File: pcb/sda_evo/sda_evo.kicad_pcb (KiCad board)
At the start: 4 copper layers, 61.5 x 105.2 mm, 136 parts, among them J1 PROG, J10 SPKR, J11 AudioJack, J2 USB_C_Receptacle_USB2.0, J3 Conn_01x40, J4 INT_EXP, J5 BATT, J9 Micro_SD_Card_Det, Q1 IRLML6302, SW1 RESET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

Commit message: Adaded part mockups. PCB is nearly finished.
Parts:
- added C52: 100n, Capacitor_SMD:C_0805_2012Metric_Pad1.18x1.45mm_HandSolder, B.Cu at (89.4, 126.1)
- added C53: 4.7u, Capacitor_SMD:C_0805_2012Metric_Pad1.18x1.45mm_HandSolder, B.Cu at (91.6, 126.1)
- C22, C23: value ?? -> 12,5p
- C3, C4: value ?? -> 12p
- J2: footprint Connector_USB:USB_C_Receptacle_XKB_U262-16XN-4BVC11 -> sda-parts:USB_C
- SW1: footprint Button_Switch_SMD:SW_SPST_B3S-1000 -> Button_Switch_SMD:SW_SPST_PTS645
- TP2: value TP_VUSB -> VUSB
- moved R11 17.5 mm to (80.2, 143.4)
- moved R10 13.0 mm to (78.2, 143.4)
- moved D5 10.3 mm to (66.8, 143.8)
- moved R9 8.45 mm to (76.2, 143.4), turned to 90 degrees
- moved TP1 7.81 mm to (81.2, 94.0)
- moved C23 4.46 mm to (97.1, 109.8)
- moved C47 4.35 mm to (62.3, 64.6), turned to 180 degrees
- moved R25 4.20 mm to (62.2, 60.4), turned to 0 degrees
- moved TP2 3.60 mm to (88.6, 134.8)
- moved TP3 2.75 mm to (85.0, 134.8)
- moved D3 2.52 mm to (80.5, 139.9), turned to 0 degrees
- moved C22 2.07 mm to (99.1, 109.8)
- moved Y2 2.07 mm to (101.4, 112.9)
- moved U9 1.88 mm to (73.0, 129.9)
- moved J9 1.80 mm to (104.5, 49.0)
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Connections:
- U10 pad 127: LCD_RST -> unconnected-(U10-PG12-Pad127)
- U10 pad 128: LCD_RD -> unconnected-(U10-PG13-Pad128)
- U10 pad 129: LCD_WR -> unconnected-(U10-PG14-Pad129)
- U10 pad 132: LCD_RS -> unconnected-(U10-PG15-Pad132)
- U10 pad 134: HALL_SENSE_R -> unconnected-(U10-PB4-Pad134)
- U10 pad 139: TS_P1 -> unconnected-(U10-PB8-Pad139)
- U10 pad 140: TS_P2 -> unconnected-(U10-PB9-Pad140)
- U10 pad 26: BTN_A -> BTN_B
- U10 pad 27: BTN_B -> BTN_A
- U10 pad 4: unconnected-(U10-PE5-Pad4) -> LCD_CS
- U10 pad 56: SIDE_BTN_4 -> TS_P1
- U10 pad 57: SIDE_BTN_5 -> TS_P2
- U10 pad 58: unconnected-(U10-PE7-Pad58) -> LCD_RST
- U10 pad 59: unconnected-(U10-PE8-Pad59) -> LCD_RD
- U10 pad 60: unconnected-(U10-PE9-Pad60) -> LCD_WR
- U10 pad 63: unconnected-(U10-PE10-Pad63) -> LCD_RS
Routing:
- net +3V3: track 0.00 -> 459.5 mm, vias 0 -> 18
- net GND: track 0.00 -> 199.2 mm, vias 0 -> 68
- net VBUS: track 0.00 -> 91.6 mm, vias 0 -> 3
- net BTN_A: track 0.00 -> 87.2 mm, vias 0 -> 1
- net RESET: track 0.00 -> 84.6 mm, vias 0 -> 3
- net BTN_UP: track 0.00 -> 84.1 mm, vias 0 -> 1
- net +BATT: track 0.00 -> 83.7 mm, vias 0 -> 5
- net BTN_DOWN: track 0.00 -> 82.9 mm, vias 0 -> 1
- net BTN_RIGHT: track 0.00 -> 78.3 mm, vias 0 -> 1
- net BTN_B: track 0.00 -> 74.8 mm, vias 0 -> 1
- net ISP_SWDIO: track 0.00 -> 69.9 mm, vias 0 -> 2
- net VD: track 0.00 -> 69.5 mm, vias 0 -> 2
- net ISP_SWCLK: track 0.00 -> 69.1 mm, vias 0 -> 2
- net BTN_LEFT: track 0.00 -> 63.3 mm, vias 0 -> 1
- net EXT_IO2: track 0.00 -> 61.8 mm, vias 0 -> 3
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- added copper zone on B.Cu, net GND
- added copper zone on F.Cu, net GND
- added copper zone on In1.Cu, net GND
- added copper zone on In2.Cu, net GND
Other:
- board text added: "Beta 0 IV. 2024 Designed in Budweis by Standa"
- board text removed: "Beta 0 Designed in Budweis by Standa"

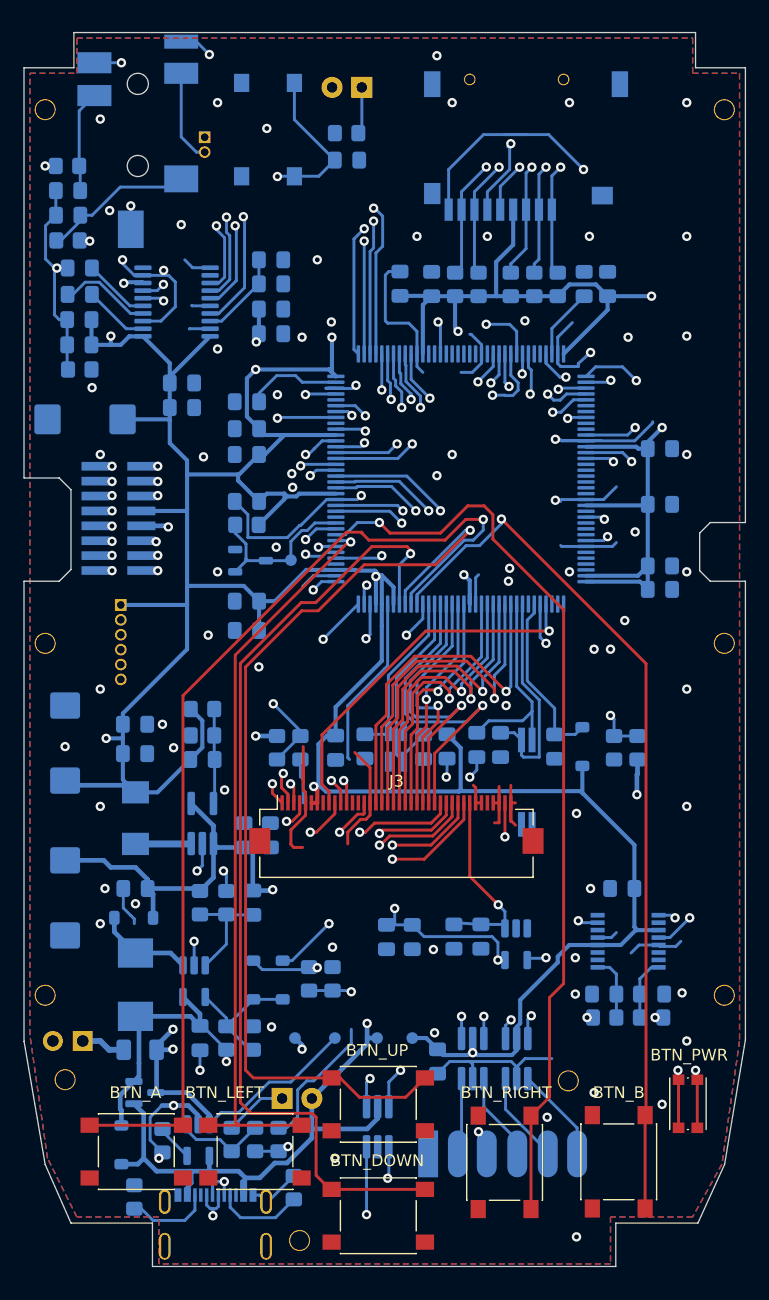
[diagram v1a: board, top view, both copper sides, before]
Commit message: i2s vias lenght matched
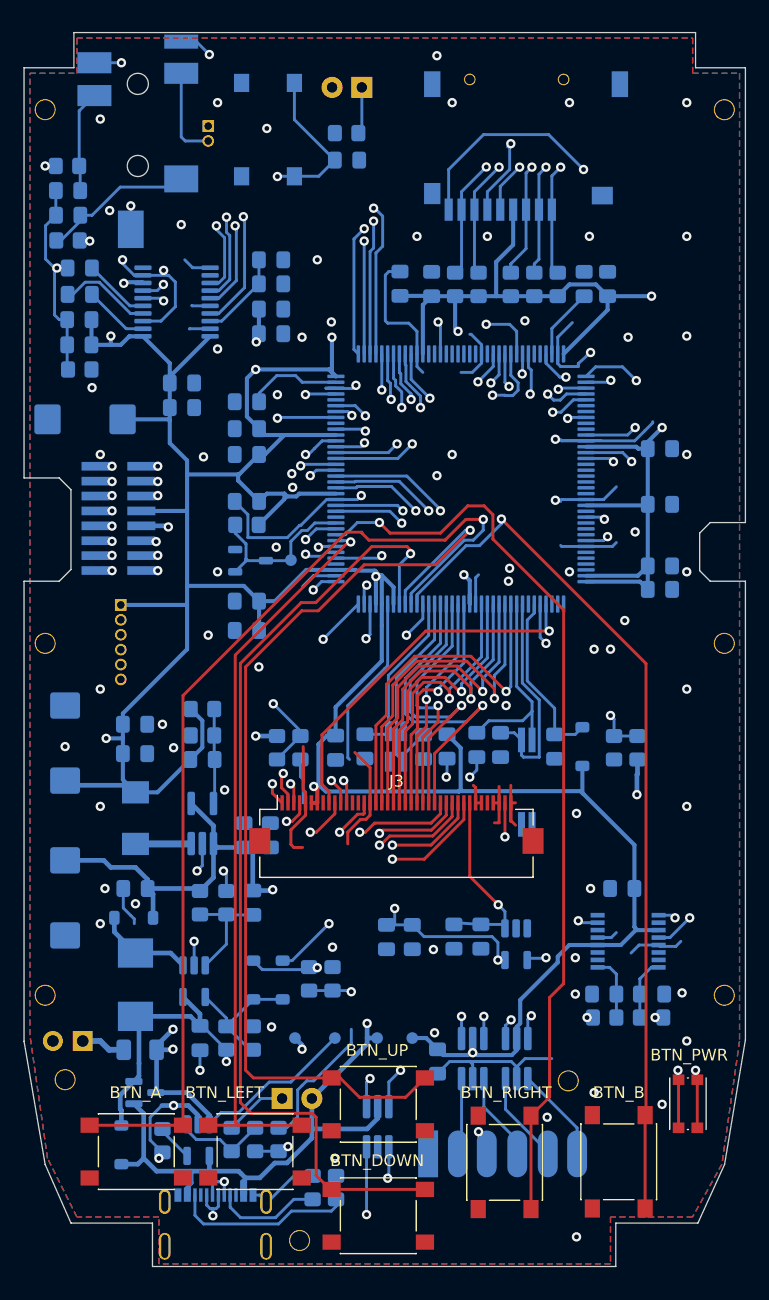
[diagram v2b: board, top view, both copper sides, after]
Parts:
- moved R28 17.2 mm to (85.1, 147.5)
- moved R29 1.60 mm to (83.1, 147.5)
- moved J10 1.00 mm to (74.2, 57.0)
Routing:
- net Net-(J2-CC2): track 7.24 -> 15.3 mm
- net PCM_CK: track 28.9 -> 33.4 mm
- net PCM_WS: track 29.9 -> 33.4 mm
- net SD_DETECT: track 40.4 -> 38.6 mm
- net Net-(J2-CC1): track 7.48 -> 9.08 mm
- net GNDA: track 54.7 -> 55.7 mm
- net PCM_MUTE: track 32.6 -> 33.4 mm
- net Net-(J10-Pin_1): track 23.3 -> 24.0 mm

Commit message: 3.5 jack moved a bit, added few holes to the casing
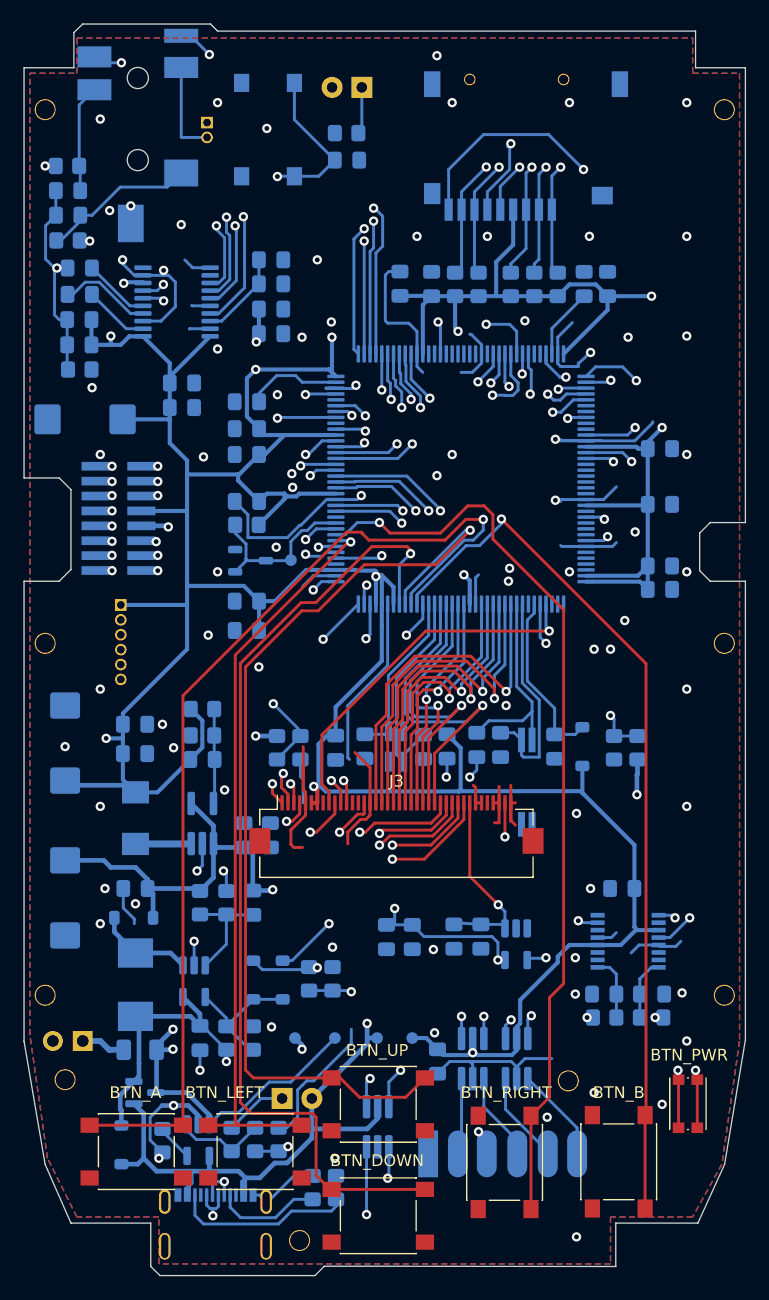
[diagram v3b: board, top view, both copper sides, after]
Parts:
- moved J11 0.50 mm to (68.2, 48.6)
- moved J10 0.32 mm to (74.1, 56.7)
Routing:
- net GNDA: track 55.7 -> 56.2 mm
- net Net-(C45-Pad1): track 8.67 -> 9.17 mm
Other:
- board size 61.5 x 105.2 mm -> 61.5 x 106.7 mm
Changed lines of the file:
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@@
   )
   (footprint "Connector_PinHeader_1.27mm:PinHeader_1x02_P1.27mm_Vertical" (layer "B.Cu")
-    (at 74.2 57 180)
+    (at 74.1 56.7 180)
     (descr "Through hole straight pin header, 1x02, 1.27mm pitch, single row")
     (tags "Through hole pin header THT 1x02 1.27mm single row")
@@
   )
   (footprint "sda-parts:3.5 Jack" (layer "B.Cu")
-    (at 68.2 49.1 90)
+    (at 68.2 48.6 90)
     (property "Sheetfile" "sda_evo.kicad_sch")
     (property "Sheetname" "")
@@
   (gr_line (start 62.75 49.025) (end 62.75 52.025)
     (stroke (width 0.1) (type default)) (layer "Edge.Cuts"))
-  (gr_line (start 69.45 150.525) (end 69.45 154.225)
+  (gr_line (start 75 48.9) (end 74.4 48.3)
+    (stroke (width 0.1) (type default)) (layer "Edge.Cuts"))
+  (gr_line (start 69.3 150.525) (end 69.3 154.225)
     (stroke (width 0.1) (type default)) (layer "Edge.Cuts"))
   (gr_line (start 116.1 91.7) (end 116.1 94.9)
@@
   (gr_line (start 118.225 145.525) (end 120 134.9)
     (stroke (width 0.1) (type default)) (layer "Edge.Cuts"))
+  (gr_line (start 84.1 154.2) (end 83.3 155)
+    (stroke (width 0.1) (type default)) (layer "Edge.Cuts"))
   (gr_line (start 60.3 145.525) (end 62.5 150.525)
     (stroke (width 0.1) (type default)) (layer "Edge.Cuts"))
@@
   (gr_line (start 58.5 135.025) (end 60.3 145.525)
     (stroke (width 0.1) (type default)) (layer "Edge.Cuts"))
+  (gr_line (start 83.3 155) (end 70.1 155)
+    (stroke (width 0.1) (type default)) (layer "Edge.Cuts"))
+  (gr_line (start 70.1 155) (end 69.3 154.225)
+    (stroke (width 0.1) (type default)) (layer "Edge.Cuts"))
   (gr_line (start 108.95 150.525) (end 115.95 150.525)
     (stroke (width 0.1) (type default)) (layer "Edge.Cuts"))
-  (gr_line (start 62.75 49.025) (end 115.75 49.025)
+  (gr_line (start 75 48.9) (end 115.75 48.9)
     (stroke (width 0.1) (type default)) (layer "Edge.Cuts"))
   (gr_line (start 115.95 150.525) (end 118.225 145.525)
@@
   (gr_line (start 58.5 52.025) (end 58.5 87)
     (stroke (width 0.1) (type default)) (layer "Edge.Cuts"))
-  (gr_line (start 115.75 49.025) (end 115.75 52.025)
+  (gr_line (start 74.4 48.3) (end 63.5 48.3)
+    (stroke (width 0.1) (type default)) (layer "Edge.Cuts"))
+  (gr_line (start 115.75 48.9) (end 115.75 52.025)
     (stroke (width 0.1) (type default)) (layer "Edge.Cuts"))
   (gr_line (start 115.75 52.025) (end 120 52.025)
     (stroke (width 0.1) (type default)) (layer "Edge.Cuts"))
-  (gr_line (start 62.5 150.525) (end 69.45 150.525)
+  (gr_line (start 62.5 150.525) (end 69.3 150.525)
+    (stroke (width 0.1) (type default)) (layer "Edge.Cuts"))
+  (gr_line (start 63.5 48.3) (end 62.75 49.025)
     (stroke (width 0.1) (type default)) (layer "Edge.Cuts"))
   (gr_line (start 117 95.8) (end 120 95.8)
@@
   (gr_line (start 58.5 95.8) (end 58.5 135.025)
     (stroke (width 0.1) (type default)) (layer "Edge.Cuts"))
-  (gr_line (start 69.45 154.225) (end 108.95 154.225)
+  (gr_line (start 84.1 154.2) (end 108.95 154.225)
     (stroke (width 0.1) (type default)) (layer "Edge.Cuts"))
   (gr_line (start 120 90.8) (end 117 90.8)
@@
   (segment (start 62 68.4) (end 61.3 69.1) (width 0.25) (layer "In1.Cu") (net 16))
   (segment (start 66.9 68.4) (end 62 68.4) (width 0.25) (layer "In1.Cu") (net 16))
-  (segment (start 73.9 58.57) (end 74.2 58.27) (width 0.25) (layer "In2.Cu") (net 16))
-  (segment (start 73.9 65.8) (end 73.9 58.57) (width 0.25) (layer "In2.Cu") (net 16))
+  (segment (start 73.9 58.17) (end 74.1 57.97) (width 0.25) (layer "In2.Cu") (net 16))
   (segment (start 70.4 69.3) (end 73.9 65.8) (width 0.25) (layer "In2.Cu") (net 16))
+  (segment (start 73.9 65.8) (end 73.9 58.17) (width 0.25) (layer "In2.Cu") (net 16))
   (segment (start 61.225 64.6) (end 60.335 65.49) (width 0.25) (layer "B.Cu") (net 16))
   (segment (start 68.6375 69.725) (end 70.825 69.725) (width 0.25) (layer "B.Cu") (net 16))
@@
   (segment (start 61.2125 64.5875) (end 61.225 64.6) (width 0.25) (layer "B.Cu") (net 16))
   (segment (start 61.5 73.5) (end 62.175 73.5) (width 0.25) (layer "B.Cu") (net 16))
+  (segment (start 71.9 57.927106) (end 71.942894 57.97) (width 0.25) (layer "B.Cu") (net 16))
+  (segment (start 71.9 52) (end 71.9 57.927106) (width 0.25) (layer "B.Cu") (net 16))
   (segment (start 62.175 73.5) (end 62.175 75.65) (width 0.25) (layer "B.Cu") (net 16))
-  (segment (start 72.242894 58.27) (end 74.2 58.27) (width 0.25) (layer "B.Cu") (net 16))
   (segment (start 61.25 69.25) (end 61.625 69.25) (width 0.25) (layer "B.Cu") (net 16))
-  (segment (start 71.9 57.927106) (end 72.242894 58.27) (width 0.25) (layer "B.Cu") (net 16))
-  (segment (start 71.9 52.5) (end 71.9 57.927106) (width 0.25) (layer "B.Cu") (net 16))
   (segment (start 62.2125 69.1) (end 62.0625 69.25) (width 0.25) (layer "B.Cu") (net 16))
   (segment (start 61.2125 62.5) (end 61.2125 64.5875) (width 0.25) (layer "B.Cu") (net 16))
@@
   (segment (start 62.0625 69.25) (end 61.625 69.25) (width 0.25) (layer "B.Cu") (net 16))
   (segment (start 70.825 69.725) (end 71.4 70.3) (width 0.25) (layer "B.Cu") (net 16))
+  (segment (start 71.942894 57.97) (end 74.1 57.97) (width 0.25) (layer "B.Cu") (net 16))
   (segment (start 62.175 77.675) (end 62.25 77.75) (width 0.25) (layer "B.Cu") (net 16))
   (segment (start 61.05 69.25) (end 61.1 69.3) (width 0.25) (layer "B.Cu") (net 16))
@@
   (segment (start 73.7125 133.7125) (end 75.75 135.75) (width 0.25) (layer "B.Cu") (net 20))
   (segment (start 66.8 142.2) (end 66.8 140.9) (width 0.4) (layer "B.Cu") (net 20))
+  (segment (start 63.2 55.2) (end 64.5 53.9) (width 0.25) (layer "B.Cu") (net 21))
   (segment (start 63.2875 60.4875) (end 63.2 60.4) (width 0.25) (layer "B.Cu") (net 21))
   (segment (start 63.2875 62.5) (end 63.2875 60.4875) (width 0.25) (layer "B.Cu") (net 21))
-  (segment (start 63.2 55.7) (end 64.5 54.4) (width 0.25) (layer "B.Cu") (net 21))
-  (segment (start 63.2 60.4) (end 63.2 55.7) (width 0.25) (layer "B.Cu") (net 21))
+  (segment (start 63.2 60.4) (end 63.2 55.2) (width 0.25) (layer "B.Cu") (net 21))
   (segment (start 74.75 111) (end 74.75 114.65) (width 0.25) (layer "B.Cu") (net 22))
   (segment (start 74.7125 110.9625) (end 74.75 111) (width 0.25) (layer "B.Cu") (net 22))
@@
   (segment (start 61.25 66.75) (end 61.644042 66.75) (width 0.25) (layer "B.Cu") (net 23))
   (segment (start 63.3 65.094042) (end 63.3 64.6) (width 0.25) (layer "B.Cu") (net 23))
+  (segment (start 70.7 62.2) (end 71.9 61) (width 0.25) (layer "B.Cu") (net 23))
   (segment (start 61.644042 66.75) (end 63.3 65.094042) (width 0.25) (layer "B.Cu") (net 23))
-  (segment (start 66.7 62.2) (end 71.2 62.2) (width 0.25) (layer "B.Cu") (net 23))
   (segment (start 63.3 64.6) (end 64.3 64.6) (width 0.25) (layer "B.Cu") (net 23))
-  (segment (start 71.2 62.2) (end 71.9 61.5) (width 0.25) (layer "B.Cu") (net 23))
   (segment (start 64.3 64.6) (end 66.7 62.2) (width 0.25) (layer "B.Cu") (net 23))
+  (segment (start 66.7 62.2) (end 70.7 62.2) (width 0.25) (layer "B.Cu") (net 23))
   (segment (start 73.5 124.2125) (end 75.75 124.2125) (width 0.25) (layer "B.Cu") (net 24))
   (segment (start 73.95 128.55) (end 75.75 126.75) (width 0.25) (layer "B.Cu") (net 24))
@@
   (via (at 66.8 51.6) (size 0.8) (drill 0.4) (layers "F.Cu" "B.Cu") (net 91))
   (via (at 67.6 63.8) (size 0.8) (drill 0.4) (layers "F.Cu" "B.Cu") (net 91))
+  (segment (start 71.1 57.95) (end 72.85 57.95) (width 0.25) (layer "In1.Cu") (net 91))
   (segment (start 68.8 63.8) (end 71.1 61.5) (width 0.25) (layer "In1.Cu") (net 91))
-  (segment (start 73.25 57.95) (end 74.2 57) (width 0.25) (layer "In1.Cu") (net 91))
   (segment (start 66.8 51.6) (end 66.8 53.803122) (width 0.25) (layer "In1.Cu") (net 91))
   (segment (start 71.1 61.5) (end 71.1 57.95) (width 0.25) (layer "In1.Cu") (net 91))
+  (segment (start 72.85 57.95) (end 74.1 56.7) (width 0.25) (layer "In1.Cu") (net 91))
   (segment (start 66.8 53.803122) (end 70.946878 57.95) (width 0.25) (layer "In1.Cu") (net 91))
   (segment (start 70.946878 57.95) (end 71.1 57.95) (width 0.25) (layer "In1.Cu") (net 91))
-  (segment (start 71.1 57.95) (end 73.25 57.95) (width 0.25) (layer "In1.Cu") (net 91))
   (segment (start 67.6 63.8) (end 68.8 63.8) (width 0.25) (layer "In1.Cu") (net 91))
-  (segment (start 64.5 51.6) (end 66.8 51.6) (width 0.25) (layer "B.Cu") (net 91))
-  (segment (start 67.6 65.8) (end 67.6 63.8) (width 0.25) (layer "B.Cu") (net 91))
+  (segment (start 67.6 65.3) (end 67.6 63.8) (width 0.25) (layer "B.Cu") (net 91))
+  (segment (start 64.5 51.1) (end 65 51.6) (width 0.25) (layer "B.Cu") (net 91))
+  (segment (start 65 51.6) (end 66.8 51.6) (width 0.25) (layer "B.Cu") (net 91))
   (via (at 93.7 51) (size 0.8) (drill 0.4) (layers "F.Cu" "B.Cu") (net 92))
   (via (at 97.9 73.9) (size 0.8) (drill 0.4) (layers "F.Cu" "B.Cu") (net 92))
@@
   (segment (start 97.9 73.9) (end 93.7 69.7) (width 0.25) (layer "In2.Cu") (net 92))
   (segment (start 93.7 69.7) (end 93.7 51) (width 0.25) (layer "In2.Cu") (net 92))
-  (segment (start 71.9 49.8) (end 73.2 49.8) (width 0.25) (layer "B.Cu") (net 92))
+  (segment (start 72.7 49.3) (end 74.3 50.9) (width 0.25) (layer "B.Cu") (net 92))
+  (segment (start 71.9 49.3) (end 72.7 49.3) (width 0.25) (layer "B.Cu") (net 92))
   (segment (start 100.5 74.5) (end 100.5 76.425) (width 0.25) (layer "B.Cu") (net 92))
-  (segment (start 73.2 49.8) (end 74.3 50.9) (width 0.25) (layer "B.Cu") (net 92))
   (segment (start 99.9 73.9) (end 100.5 74.5) (width 0.25) (layer "B.Cu") (net 92))
   (segment (start 97.9 73.9) (end 99.9 73.9) (width 0.25) (layer "B.Cu") (net 92))

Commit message: PCB: footprints adjusted
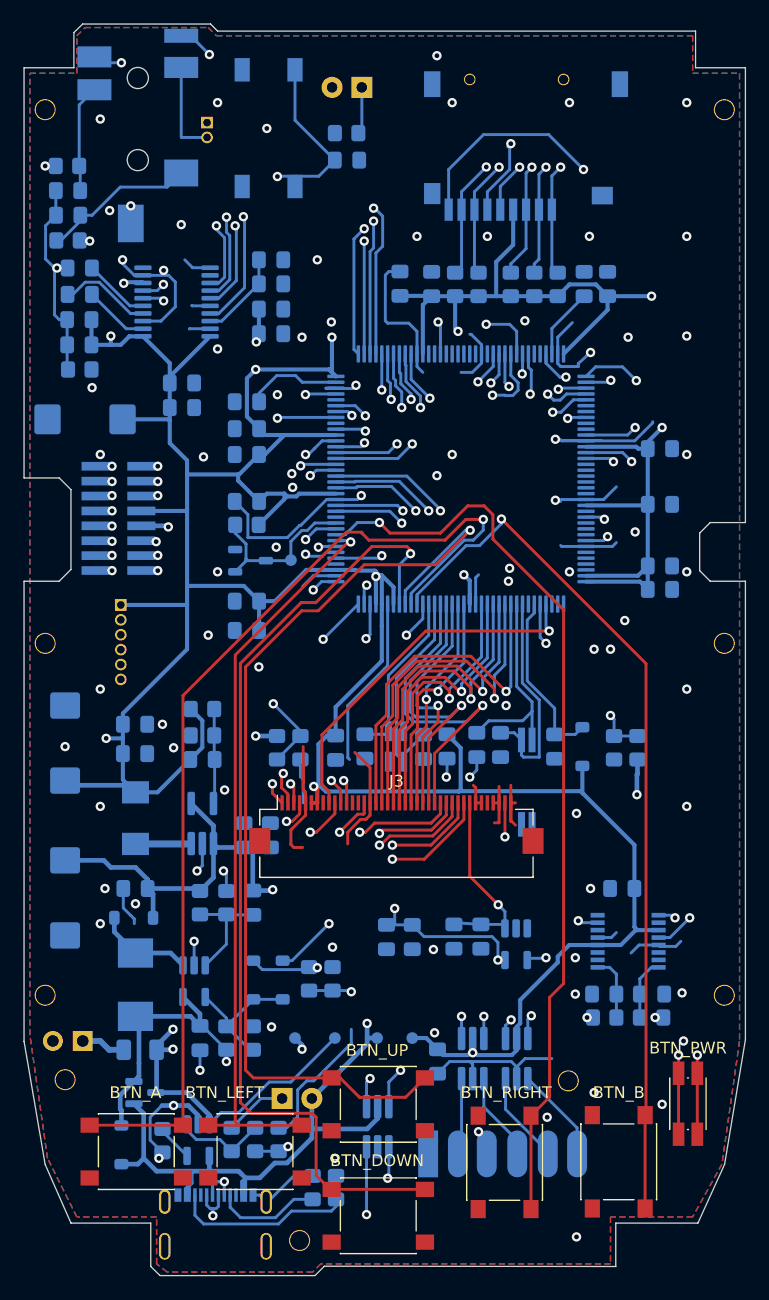
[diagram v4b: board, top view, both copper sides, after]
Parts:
- SW1: footprint Button_Switch_SMD:SW_SPST_PTS645 -> sda-parts:SW_SPST_RESET
- SW8: footprint Button_Switch_SMD:SW_Push_1P1T_NO_CK_KMR2 -> sda-parts:SW_Push_1P1T_NO_CK_KMR2_PWR
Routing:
- net RESET: track 84.6 -> 87.4 mm
- net VD: track 69.5 -> 68.3 mm
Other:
- board text added: "Beta 0 V. 2024 Designed in Budweis by Standa"
- board text removed: "Beta 0 IV. 2024 Designed in Budweis by Standa"
